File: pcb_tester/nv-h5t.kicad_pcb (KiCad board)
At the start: 2 copper layers, 8 x 50 mm, 16 parts, among them J1 PSH02-03, U1 ATtiny25-20SS

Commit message: NV-H5B tester -> NV-H5T.
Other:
- board text added: "NV-H5t v1.0"
- board text removed: "NV-H5b tester v1.0"
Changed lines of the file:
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@@
     (effects (font (size 1.5 1.5) (thickness 0.1)) (justify mirror))
   )
-  (gr_text "NV-H5b\ntester\nv1.0" (at 123.952 120.462) (layer "B.SilkS")
+  (gr_text "NV-H5t\nv1.0" (at 123.952 120.462) (layer "B.SilkS")
     (effects (font (size 1 1) (thickness 0.1)) (justify mirror))
   )

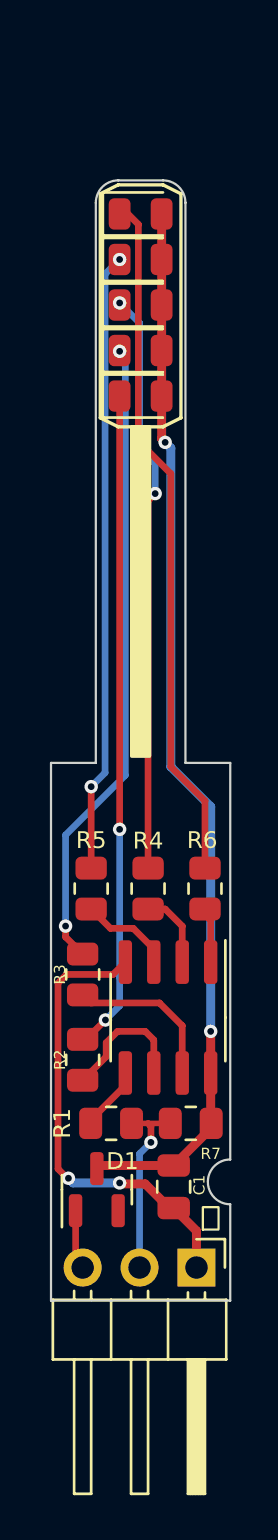
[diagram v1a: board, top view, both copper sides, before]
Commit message: Add 3V3 stabilizer, so NV-H5T supports both 5V & 12V power supply.
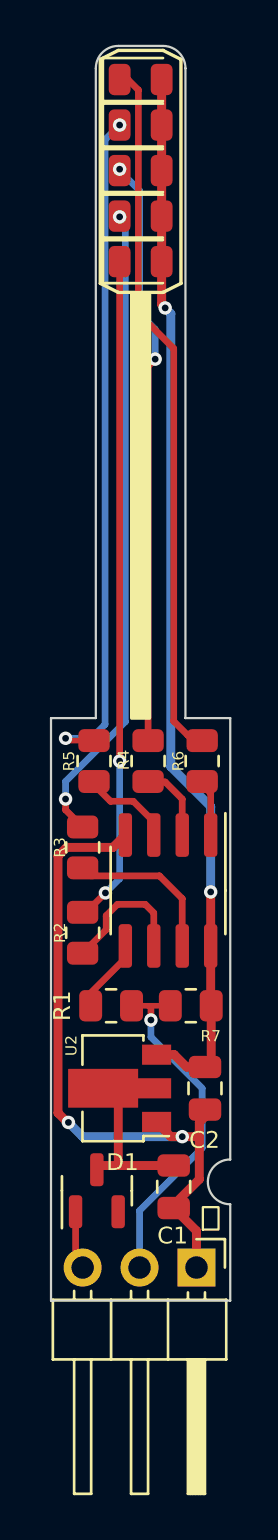
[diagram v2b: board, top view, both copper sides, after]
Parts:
- added C2: 1u, Capacitor_SMD:C_0805_2012Metric, F.Cu at (126.9, 120.5)
- added U2: AP2204RA-3.3, Package_TO_SOT_SMD:SOT-89-3, F.Cu at (123.1, 120.5)
- moved D2 6.00 mm to (124.0, 83.6)
- moved D3 6.00 mm to (124.0, 81.6)
- moved D4 6.00 mm to (124.0, 79.6)
- moved D5 6.00 mm to (124.0, 77.5)
- moved D6 6.00 mm to (124.0, 75.5)
- moved R5 5.69 mm to (121.9, 105.9)
- moved R6 5.69 mm to (126.7, 105.9)
- moved R4 5.69 mm to (124.3, 105.9)
- moved R2 5.67 mm to (121.4, 113.6)
- moved U1 5.67 mm to (125.2, 111.7)
- moved R3 5.67 mm to (121.4, 109.8)
- moved R1 5.25 mm to (122.7, 116.8)
- moved R7 5.25 mm to (126.2, 116.8)
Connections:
- C1 pad 1: VCC -> Net-(D1-Pad3)
- D1 pad 3: VCC -> Net-(D1-Pad3)
- D2 pad 2: VCC -> +3V3
- D3 pad 2: VCC -> +3V3
- D4 pad 2: VCC -> +3V3
- D5 pad 2: VCC -> +3V3
- D6 pad 2: VCC -> +3V3
- R7 pad 1: VCC -> +3V3
- U1 pad 8: VCC -> +3V3
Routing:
- net VCC: track 47.6 -> 0.00 mm, vias 2 -> 0
- net +3V3: track 0.00 -> 47.2 mm, vias 0 -> 2
- net GND: track 20.7 -> 31.3 mm
- net Net-(D1-Pad3): track 0.00 -> 7.00 mm
- net /DATA_IN: track 8.43 -> 15.4 mm
- net /LED_GR: track 27.7 -> 30.4 mm
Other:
- board size 8 x 50 mm -> 8 x 56 mm
- board text added: "JH 2023 KMŽ Brno I"

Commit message: Make panel.
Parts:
- added REF**: Tab, kikit:Tab, F.Cu at (126.2, 84.5)
- added REF**: Tab, kikit:Tab, F.Cu at (128.3, 115.7)
- added REF**: Tab, kikit:Tab, F.Cu at (121.8, 84.5)
- added REF**: Tab, kikit:Tab, F.Cu at (119.8, 115.7)
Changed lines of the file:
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@@
   (net 16 "/dLED_YEL_TOP")
   (net 17 "+3V3")
+  (footprint "kikit:Tab" (layer "F.Cu")
+    (at 126.238 84.455 180)
+    (descr "A symbol representing annotation for tab placement")
+    (attr exclude_from_pos_files exclude_from_bom)
+    (fp_text reference "REF**" (at 0 -2) (layer "F.SilkS") hide
+      (effects (font (size 1 1) (thickness 0.15)))
+    )
+    (fp_text value "Tab" (at -2.75 -1) (layer "Dwgs.User")
+      (effects (font (size 1.2 1.2) (thickness 0.2)))
+    )
+    (fp_text user "KIKIT: width: 2mm" (at -5.5 0 90) (layer "Dwgs.User")
+      (effects (font (size 1 1) (thickness 0.15)))
+    )
+    (fp_line (start 0.25 0) (end -2.75 0) (layer "Dwgs.User") (width 0.3))
+    (fp_line (start 0.25 1) (end 0.25 -1) (layer "Dwgs.User") (width 0.3))
+    (fp_line (start 0.25 0) (end -0.75 -1) (layer "Dwgs.User") (width 0.3))
+    (fp_line (start 0.25 0) (end -0.75 1) (layer "Dwgs.User") (width 0.3))
+  )
   (footprint "Resistor_SMD:R_0805_2012Metric" (layer "F.Cu")
     (at 122.682 116.84 180)
@@
       (rotate (xyz 0 0 0))
     )
+  )
+  (footprint "kikit:Tab" (layer "F.Cu")
+    (at 128.27 115.697 180)
+    (descr "A symbol representing annotation for tab placement")
+    (attr exclude_from_pos_files exclude_from_bom)
+    (fp_text reference "REF**" (at 0 -2) (layer "F.SilkS") hide
+      (effects (font (size 1 1) (thickness 0.15)))
+    )
+    (fp_text value "Tab" (at -2.75 -1) (layer "Dwgs.User")
+      (effects (font (size 1.2 1.2) (thickness 0.2)))
+    )
+    (fp_text user "KIKIT: width: 3mm" (at -5.5 0 90) (layer "Dwgs.User")
+      (effects (font (size 1 1) (thickness 0.15)))
+    )
+    (fp_line (start 0.25 0) (end -2.75 0) (layer "Dwgs.User") (width 0.3))
+    (fp_line (start 0.25 1) (end 0.25 -1) (layer "Dwgs.User") (width 0.3))
+    (fp_line (start 0.25 0) (end -0.75 -1) (layer "Dwgs.User") (width 0.3))
+    (fp_line (start 0.25 0) (end -0.75 1) (layer "Dwgs.User") (width 0.3))
   )
   (footprint "LED_SMD:LED_0805_2012Metric" (layer "F.Cu")
@@
     )
   )
+  (footprint "kikit:Tab" (layer "F.Cu")
+    (at 121.793 84.455)
+    (descr "A symbol representing annotation for tab placement")
+    (attr exclude_from_pos_files exclude_from_bom)
+    (fp_text reference "REF**" (at 0 -2) (layer "F.SilkS") hide
+      (effects (font (size 1 1) (thickness 0.15)))
+    )
+    (fp_text value "Tab" (at -2.75 -1) (layer "Dwgs.User")
+      (effects (font (size 1.2 1.2) (thickness 0.2)))
+    )
+    (fp_text user "KIKIT: width: 2mm" (at -5.5 0 90) (layer "Dwgs.User")
+      (effects (font (size 1 1) (thickness 0.15)))
+    )
+    (fp_line (start 0.25 0) (end -2.75 0) (layer "Dwgs.User") (width 0.3))
+    (fp_line (start 0.25 1) (end 0.25 -1) (layer "Dwgs.User") (width 0.3))
+    (fp_line (start 0.25 0) (end -0.75 -1) (layer "Dwgs.User") (width 0.3))
+    (fp_line (start 0.25 0) (end -0.75 1) (layer "Dwgs.User") (width 0.3))
+  )
   (footprint "Resistor_SMD:R_0805_2012Metric" (layer "F.Cu")
     (at 121.412 109.772 -90)
@@
     )
   )
+  (footprint "kikit:Tab" (layer "F.Cu")
+    (at 119.761 115.697)
+    (descr "A symbol representing annotation for tab placement")
+    (attr exclude_from_pos_files exclude_from_bom)
+    (fp_text reference "REF**" (at 0 -2) (layer "F.SilkS") hide
+      (effects (font (size 1 1) (thickness 0.15)))
+    )
+    (fp_text value "Tab" (at -2.75 -1) (layer "Dwgs.User")
+      (effects (font (size 1.2 1.2) (thickness 0.2)))
+    )
+    (fp_text user "KIKIT: width: 3mm" (at -5.5 0 90) (layer "Dwgs.User")
+      (effects (font (size 1 1) (thickness 0.15)))
+    )
+    (fp_line (start 0.25 0) (end -2.75 0) (layer "Dwgs.User") (width 0.3))
+    (fp_line (start 0.25 1) (end 0.25 -1) (layer "Dwgs.User") (width 0.3))
+    (fp_line (start 0.25 0) (end -0.75 -1) (layer "Dwgs.User") (width 0.3))
+    (fp_line (start 0.25 0) (end -0.75 1) (layer "Dwgs.User") (width 0.3))
+  )
   (footprint "LED_SMD:LED_0805_2012Metric" (layer "F.Cu")
